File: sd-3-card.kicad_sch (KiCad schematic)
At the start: 20 parts, among them J2 1140084168, Q1 BSS123, Q2 AO3401A, U5 NVT4858HKZ, U6 TPS2116DRLR

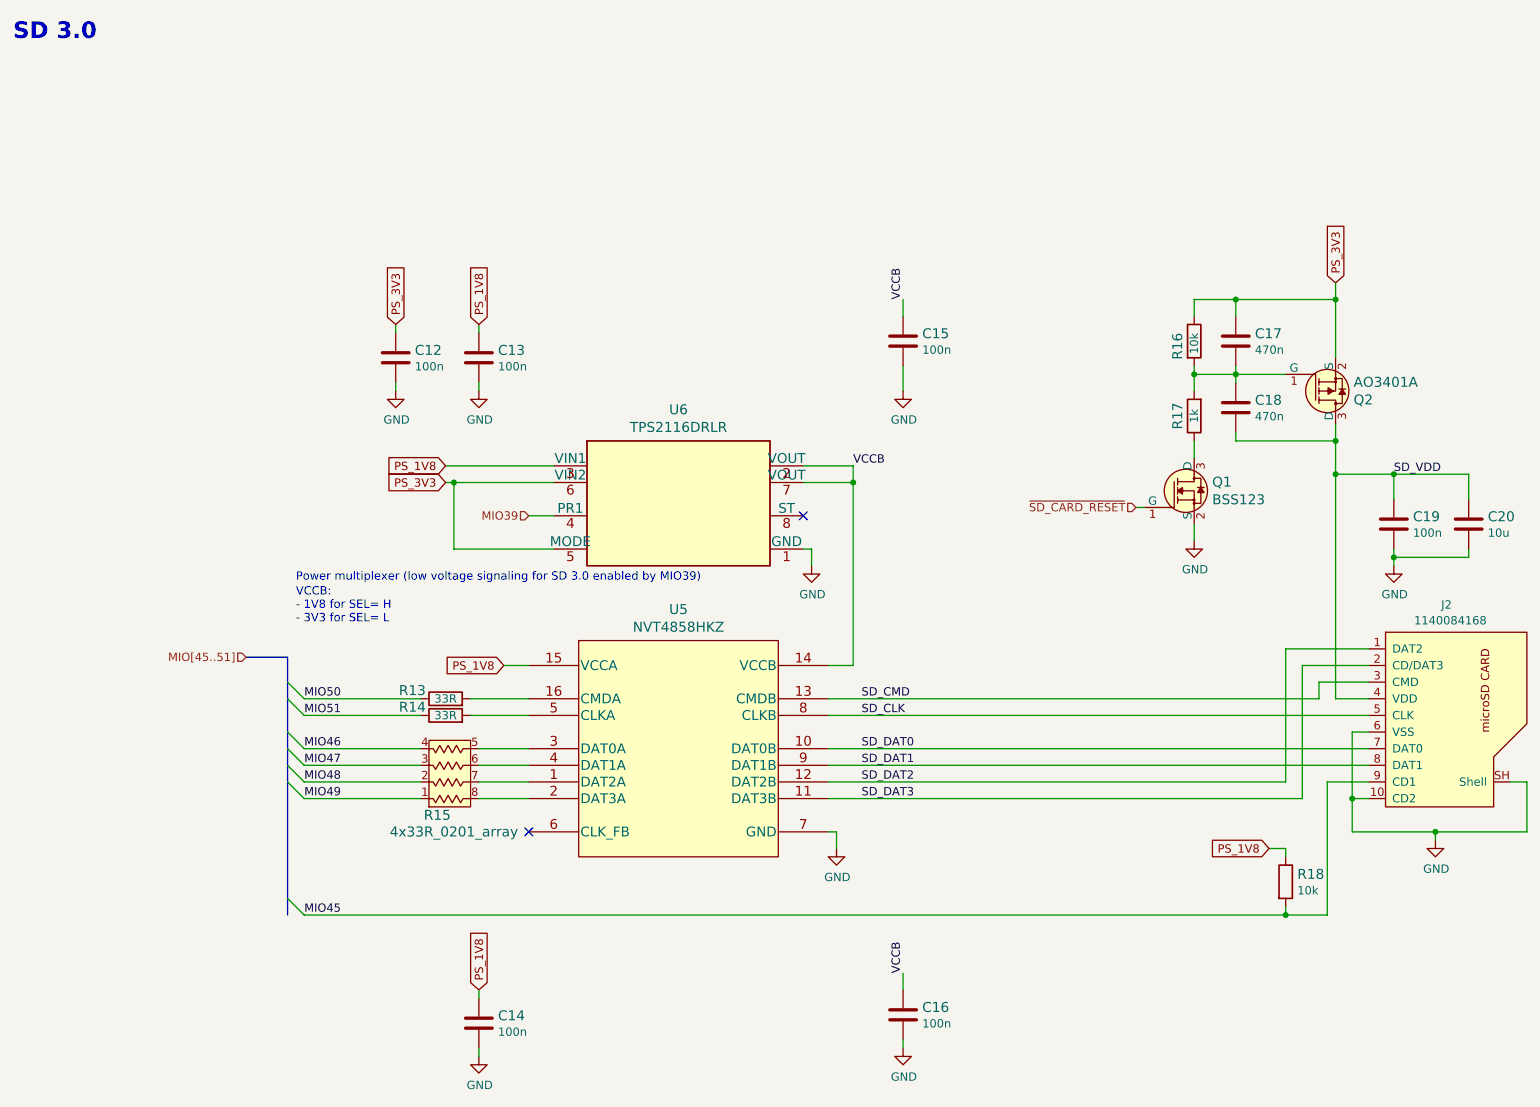
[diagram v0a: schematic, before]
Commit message: Added cosmetic changes to schematics (e.g. position of labels, designators)
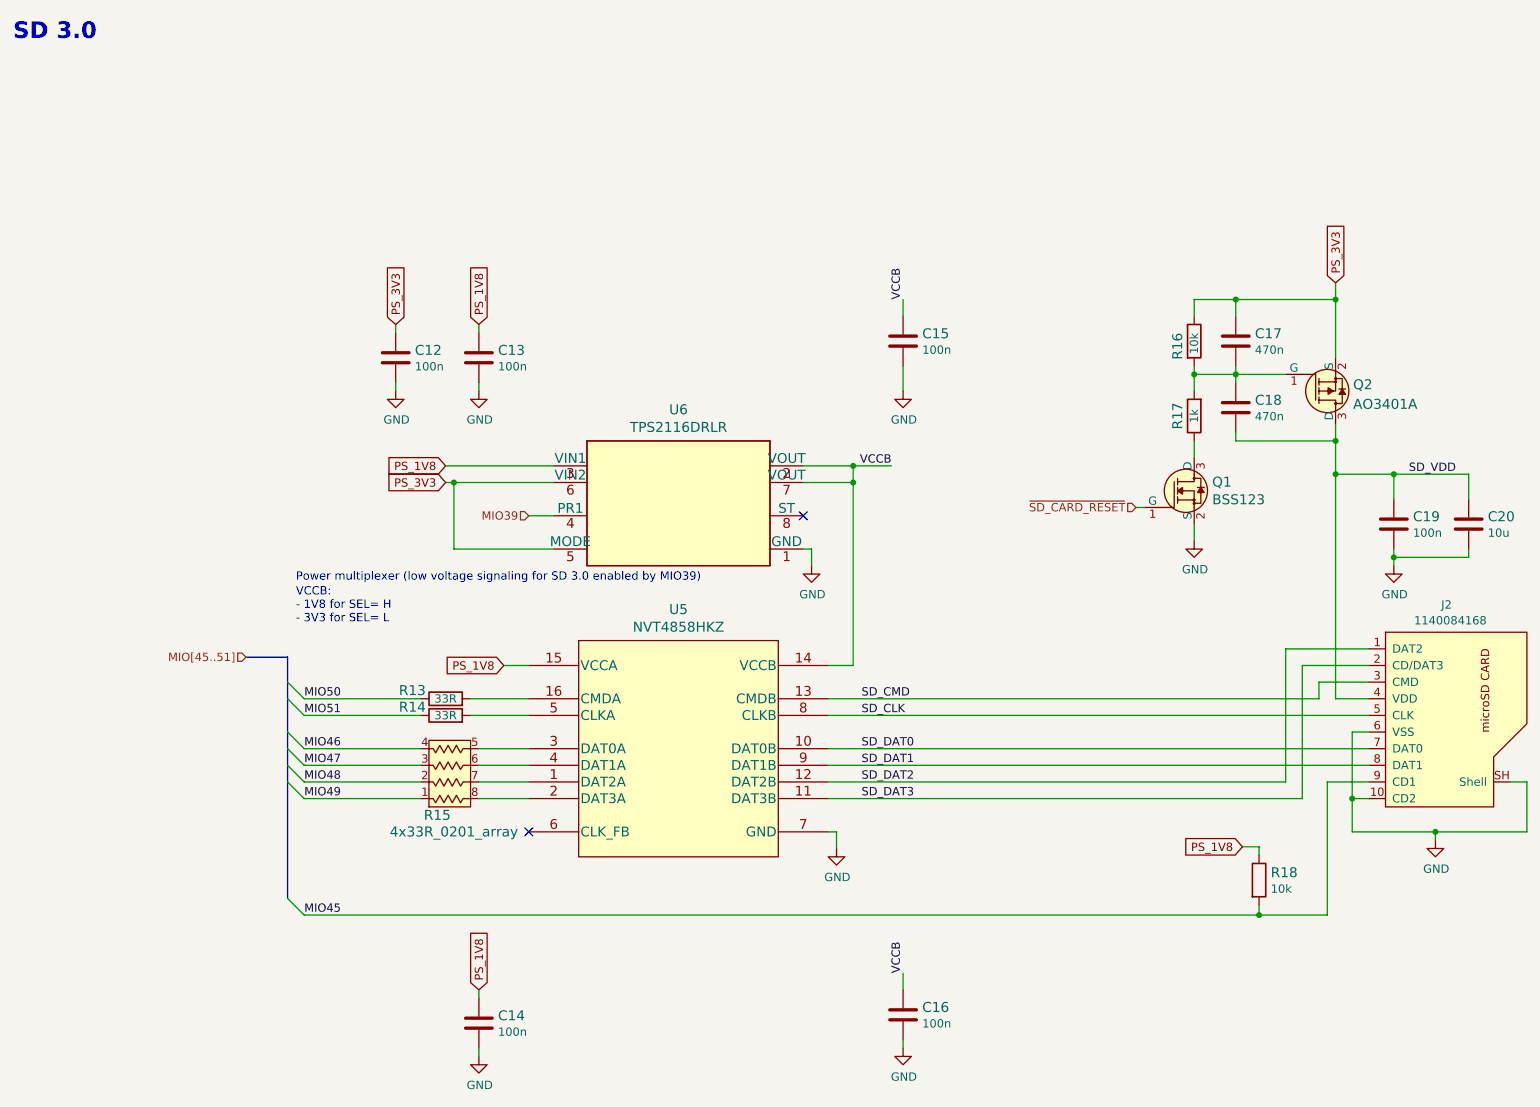
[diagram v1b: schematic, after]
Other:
- moved on the sheet: R18
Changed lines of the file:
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@@
   (junction (at 217.17 58.42) (diameter 0) (color 0 0 0 0)
   )
+  (junction (at 143.51 83.82) (diameter 0) (color 0 0 0 0)
+  )
   (junction (at 226.06 97.79) (diameter 0) (color 0 0 0 0)
   )
-  (junction (at 217.17 85.09) (diameter 0) (color 0 0 0 0)
+  (junction (at 205.486 152.4) (diameter 0) (color 0 0 0 0)
   )
-  (junction (at 209.55 152.4) (diameter 0) (color 0 0 0 0)
+  (junction (at 217.17 85.09) (diameter 0) (color 0 0 0 0)
   )
   (junction (at 226.06 85.09) (diameter 0) (color 0 0 0 0)
@@
     (stroke (width 0) (type default) (color 0 0 0 0))
   )
-  (bus (pts (xy 57.15 149.86) (xy 57.15 152.4))
-    (stroke (width 0) (type default) (color 0 0 0 0))
-  )
-  (wire (pts (xy 209.55 152.4) (xy 209.55 151.13))
+  (wire (pts (xy 205.486 150.876) (xy 205.486 152.4))
     (stroke (width 0) (type default) (color 0 0 0 0))
   )
@@
     (stroke (width 0) (type default) (color 0 0 0 0))
   )
-  (wire (pts (xy 209.55 143.51) (xy 209.55 142.24))
+  (wire (pts (xy 205.486 143.256) (xy 205.486 141.986))
     (stroke (width 0) (type default) (color 0 0 0 0))
   )
@@
     (stroke (width 0) (type default) (color 0 0 0 0))
   )
+  (wire (pts (xy 143.51 83.82) (xy 143.51 86.36))
+    (stroke (width 0) (type default) (color 0 0 0 0))
+  )
   (wire (pts (xy 137.16 99.06) (xy 137.16 96.52))
     (stroke (width 0) (type default) (color 0 0 0 0))
@@
     (stroke (width 0) (type default) (color 0 0 0 0))
   )
-  (wire (pts (xy 209.55 152.4) (xy 215.9 152.4))
+  (wire (pts (xy 59.69 152.4) (xy 205.486 152.4))
     (stroke (width 0) (type default) (color 0 0 0 0))
   )
@@
     (stroke (width 0) (type default) (color 0 0 0 0))
   )
+  (wire (pts (xy 143.51 83.82) (xy 149.352 83.82))
+    (stroke (width 0) (type default) (color 0 0 0 0))
+  )
   (wire (pts (xy 219.71 124.46) (xy 219.71 134.62))
     (stroke (width 0) (type default) (color 0 0 0 0))
@@
     (stroke (width 0) (type default) (color 0 0 0 0))
   )
-  (wire (pts (xy 59.69 152.4) (xy 209.55 152.4))
-    (stroke (width 0) (type default) (color 0 0 0 0))
-  )
   (wire (pts (xy 209.55 111.76) (xy 222.25 111.76))
     (stroke (width 0) (type default) (color 0 0 0 0))
@@
     (stroke (width 0) (type default) (color 0 0 0 0))
   )
-  (wire (pts (xy 207.01 142.24) (xy 209.55 142.24))
+  (wire (pts (xy 202.946 141.986) (xy 205.486 141.986))
     (stroke (width 0) (type default) (color 0 0 0 0))
   )
@@
     (stroke (width 0) (type default) (color 0 0 0 0))
   )
-  (wire (pts (xy 143.51 83.82) (xy 143.51 86.36))
-    (stroke (width 0) (type default) (color 0 0 0 0))
-  )
   (wire (pts (xy 195.58 95.25) (xy 195.58 92.71))
     (stroke (width 0) (type default) (color 0 0 0 0))
@@
     (stroke (width 0) (type default) (color 0 0 0 0))
   )
+  (wire (pts (xy 205.486 152.4) (xy 215.9 152.4))
+    (stroke (width 0) (type default) (color 0 0 0 0))
+  )
   (bus (pts (xy 57.15 132.08) (xy 57.15 149.86))
     (stroke (width 0) (type default) (color 0 0 0 0))
@@
     (effects (font (size 1.27 1.27)) (justify left bottom))
   )
-  (label "SD_VDD" (at 226.06 85.09 0)
+  (label "SD_VDD" (at 228.346 85.09 0)
     (effects (font (size 1.27 1.27)) (justify left bottom))
   )
-  (label "VCCB" (at 143.51 83.82 0)
-    (effects (font (size 1.27 1.27)) (justify left bottom))
+  (label "VCCB" (at 149.352 83.82 180)
+    (effects (font (size 1.27 1.27)) (justify right bottom))
   )
   (label "MIO46" (at 59.69 127 0)
@@
     )
   )
-  (global_label "PS_1V8" (shape input) (at 207.01 142.24 180) (fields_autoplaced)
+  (global_label "PS_1V8" (shape input) (at 202.946 141.986 180) (fields_autoplaced)
     (effects (font (size 1.27 1.27)) (justify right))
-    (property "Intersheet References" "${INTERSHEET_REFS}" (id 0) (at 0 0 0)
+    (property "Intersheet References" "${INTERSHEET_REFS}" (id 0) (at -4.064 -0.254 0)
       (effects (font (size 1.27 1.27)) hide)
     )
@@
     (pin "1")
   )
-  (symbol (lib_id "kria-k26-devboard:R_10k_0402") (at 209.55 147.32 270) (unit 1)
+  (symbol (lib_id "kria-k26-devboard:R_10k_0402") (at 205.486 147.066 270) (unit 1)
     (in_bom yes) (on_board yes)
-    (property "Reference" "R18" (id 0) (at 211.328 146.177 90)
+    (property "Reference" "R18" (id 0) (at 207.264 145.923 90)
       (effects (font (size 1.524 1.524)) (justify left))
     )
-    (property "Value" "R_10k_0402" (id 1) (at 205.74 147.32 0)
+    (property "Value" "R_10k_0402" (id 1) (at 201.676 147.066 0)
       (effects (font (size 1.524 1.524)) hide)
     )
-    (property "Footprint" "kria-k26-devboard-footprints:0402-res" (id 2) (at 214.63 152.4 0)
+    (property "Footprint" "kria-k26-devboard-footprints:0402-res" (id 2) (at 210.566 152.146 0)
       (effects (font (size 1.524 1.524)) (justify left) hide)
     )
-    (property "Datasheet" "" (id 3) (at 209.55 147.32 0)
+    (property "Datasheet" "" (id 3) (at 205.486 147.066 0)
       (effects (font (size 1.27 1.27)) hide)
     )
-    (property "Manufacturer" "VISHAY" (id 4) (at 219.71 152.4 0)
+    (property "Manufacturer" "VISHAY" (id 4) (at 215.646 152.146 0)
       (effects (font (size 1.524 1.524)) (justify left) hide)
     )
-    (property "MPN" "CRCW040210K0FKEDHP" (id 5) (at 217.17 152.4 0)
+    (property "MPN" "CRCW040210K0FKEDHP" (id 5) (at 213.106 152.146 0)
       (effects (font (size 1.524 1.524)) (justify left) hide)
     )
-    (property "Val" "10k" (id 6) (at 211.328 148.6662 90)
+    (property "Val" "10k" (id 6) (at 207.264 148.4122 90)
       (effects (font (size 1.27 1.27)) (justify left))
     )
@@
   )
   (symbol (lib_id "kria-k26-devboard:AO3401A") (at 217.17 72.39 0) (mirror x) (unit 1)
-    (in_bom yes) (on_board yes)
-    (property "Reference" "Q2" (id 0) (at 219.9132 73.7362 0)
+    (in_bom yes) (on_board yes) (fields_autoplaced)
+    (property "Reference" "Q2" (id 0) (at 219.837 71.4138 0)
       (effects (font (size 1.524 1.524)) (justify left))
     )
-    (property "Value" "AO3401A" (id 1) (at 219.9132 71.0438 0)
+    (property "Value" "AO3401A" (id 1) (at 219.837 74.4072 0)
       (effects (font (size 1.524 1.524)) (justify left))
     )

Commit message: Bump date and revision
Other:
- title: SD 3.0 card -> Kria K26 Devboard
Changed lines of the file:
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@@
   (paper "A4")
   (title_block
-    (title "SD 3.0 card")
-    (date "2022-07-25")
-    (rev "1.1.0")
+    (title "Kria K26 Devboard")
+    (date "2023-02-15")
+    (rev "1.1.1")
     (comment 1 "www.antmicro.com")
     (comment 2 "Antmicro Ltd.")

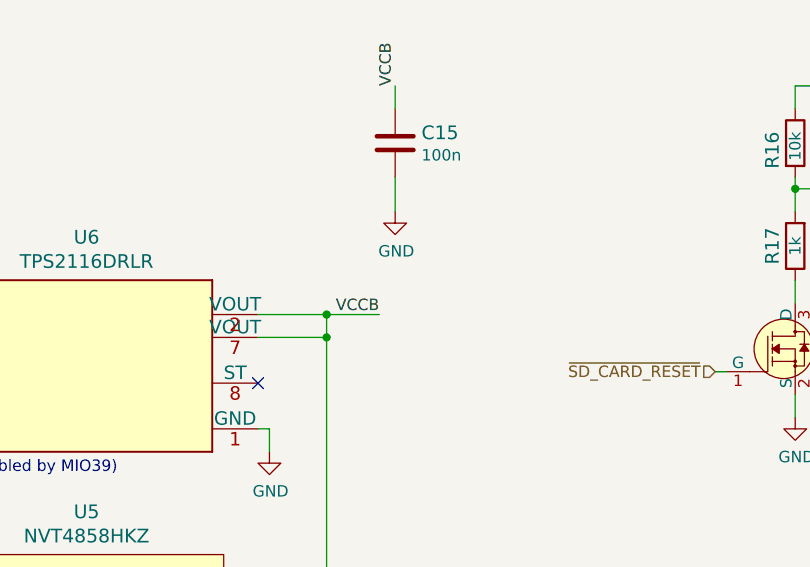
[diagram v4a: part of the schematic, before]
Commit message: Add mandatory pullup to TPS2116 status signal
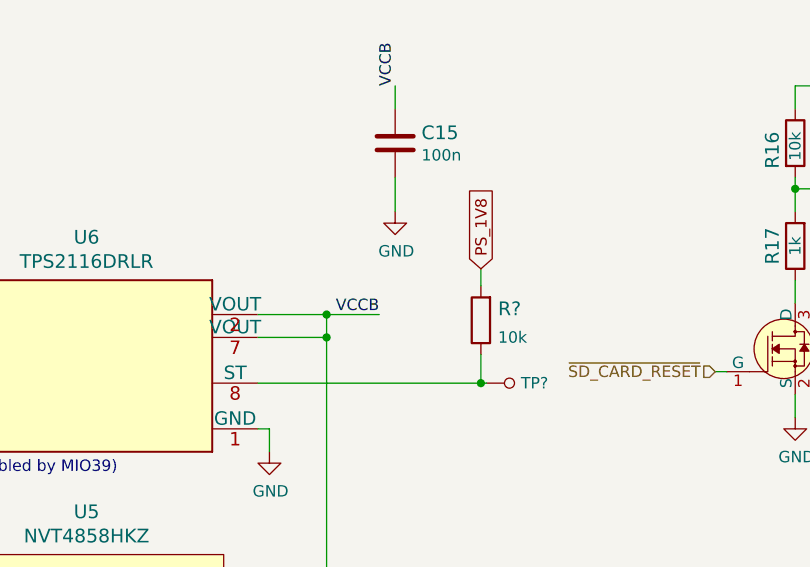
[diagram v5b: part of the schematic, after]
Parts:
- added R?: R_10k_0402, antmicro-footprints:0402-res, symbol antmicroResistors0402:R_10k_0402
- added TP?: TP_SMD_0_75MM, antmicro-footprints:Testpoint_smd_0_75mm, symbol antmicroTestPoints:TP_SMD_0_75MM
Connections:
- net PS_1V8: now also R?.2
- net at U6.8 (ST): now also R?.1, TP?.1
- no-connect marks 2 -> 1
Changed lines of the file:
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@@
   (junction (at 232.41 139.7) (diameter 0) (color 0 0 0 0)
   )
+  (junction (at 160.655 91.44) (diameter 0) (color 0 0 0 0)
+  )
   (junction (at 143.51 86.36) (diameter 0) (color 0 0 0 0)
   )
@@
   )
   (no_connect (at 93.98 139.7))
-  (no_connect (at 135.89 91.44))
   (bus_entry (at 57.15 116.84) (size 2.54 2.54)
     (stroke (width 0) (type default) (color 0 0 0 0))
@@
     (stroke (width 0) (type default) (color 0 0 0 0))
   )
+  (wire (pts (xy 160.655 91.44) (xy 160.655 88.265))
+    (stroke (width 0) (type default) (color 0 0 0 0))
+  )
   (wire (pts (xy 143.51 83.82) (xy 143.51 86.36))
     (stroke (width 0) (type default) (color 0 0 0 0))
@@
     (stroke (width 0) (type default) (color 0 0 0 0))
   )
+  (wire (pts (xy 135.89 91.44) (xy 160.655 91.44))
+    (stroke (width 0) (type default) (color 0 0 0 0))
+  )
   (wire (pts (xy 195.58 69.85) (xy 201.93 69.85))
     (stroke (width 0) (type default) (color 0 0 0 0))
@@
     (stroke (width 0) (type default) (color 0 0 0 0))
   )
+  (wire (pts (xy 160.655 91.44) (xy 161.29 91.44))
+    (stroke (width 0) (type default) (color 0 0 0 0))
+  )
   (bus (pts (xy 57.15 119.38) (xy 57.15 124.46))
     (stroke (width 0) (type default) (color 0 0 0 0))
@@
     (stroke (width 0) (type default) (color 0 0 0 0))
   )
+  (wire (pts (xy 160.655 78.74) (xy 160.655 80.645))
+    (stroke (width 0) (type default) (color 0 0 0 0))
+  )
   (wire (pts (xy 195.58 72.39) (xy 195.58 69.85))
     (stroke (width 0) (type default) (color 0 0 0 0))
@@
     )
   )
+  (global_label "PS_1V8" (shape input) (at 160.655 78.74 90) (fields_autoplaced)
+    (effects (font (size 1.27 1.27)) (justify left))
+    (property "Intersheet References" "${INTERSHEET_REFS}" (id 0) (at 244.475 -2.54 0)
+      (effects (font (size 1.27 1.27)) hide)
+    )
+  )
   (global_label "PS_3V3" (shape input) (at 73.66 62.23 90) (fields_autoplaced)
     (effects (font (size 1.27 1.27)) (justify left))
@@
     )
     (pin "1")
+  )
+  (symbol (lib_id "antmicroResistors0402:R_10k_0402") (at 160.655 84.455 90) (unit 1)
+    (in_bom yes) (on_board yes) (fields_autoplaced)
+    (property "Reference" "R?" (id 0) (at 162.56 83.185 90)
+      (effects (font (size 1.524 1.524)) (justify right))
+    )
+    (property "Value" "R_10k_0402" (id 1) (at 164.465 84.455 0)
+      (effects (font (size 1.524 1.524)) hide)
+    )
+    (property "Footprint" "antmicro-footprints:0402-res" (id 2) (at 155.575 79.375 0)
+      (effects (font (size 1.524 1.524)) (justify left) hide)
+    )
+    (property "Datasheet" "" (id 3) (at 160.655 84.455 0)
+      (effects (font (size 1.27 1.27)) hide)
+    )
+    (property "Manufacturer" "VISHAY" (id 4) (at 150.495 79.375 0)
+      (effects (font (size 1.524 1.524)) (justify left) hide)
+    )
+    (property "MPN" "CRCW040210K0FKEDHP" (id 5) (at 153.035 79.375 0)
+      (effects (font (size 1.524 1.524)) (justify left) hide)
+    )
+    (property "Val" "10k" (id 6) (at 162.56 86.3599 90)
+      (effects (font (size 1.27 1.27)) (justify right))
+    )
+    (pin "1")
+    (pin "2")
+  )
+  (symbol (lib_id "antmicroTestPoints:TP_SMD_0_75MM") (at 163.83 91.44 90) (unit 1)
+    (in_bom yes) (on_board yes) (fields_autoplaced)
+    (property "Reference" "TP?" (id 0) (at 165.1 91.4399 90)
+      (effects (font (size 1.27 1.27)) (justify right))
+    )
+    (property "Value" "TP_SMD_0_75MM" (id 1) (at 166.37 91.44 0)
+      (effects (font (size 1.27 1.27)) hide)
+    )
+    (property "Footprint" "antmicro-footprints:Testpoint_smd_0_75mm" (id 2) (at 158.75 86.36 0)
+      (effects (font (size 1.524 1.524)) (justify left) hide)
+    )
+    (property "Datasheet" "" (id 3) (at 156.21 86.36 0)
+      (effects (font (size 1.524 1.524)) (justify left) hide)
+    )
+    (pin "1")

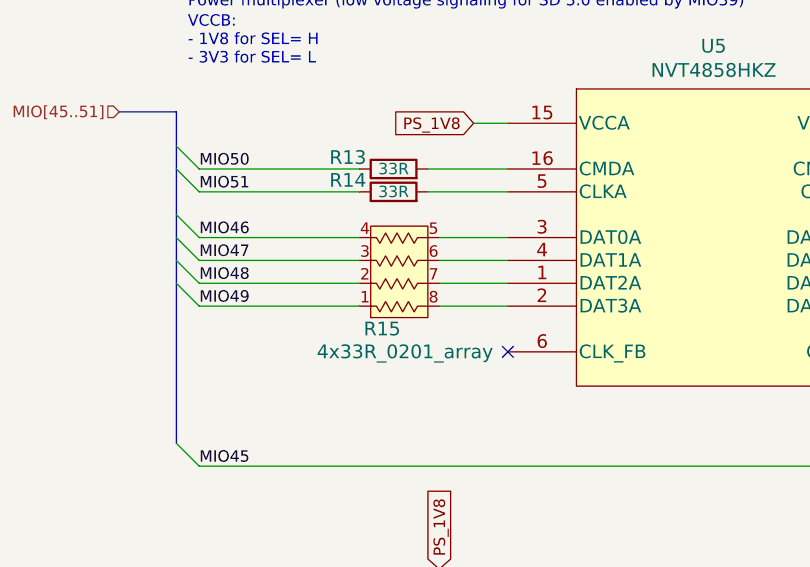
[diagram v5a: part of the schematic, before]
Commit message: Export schematic changes to PCB, fix R15 footprint
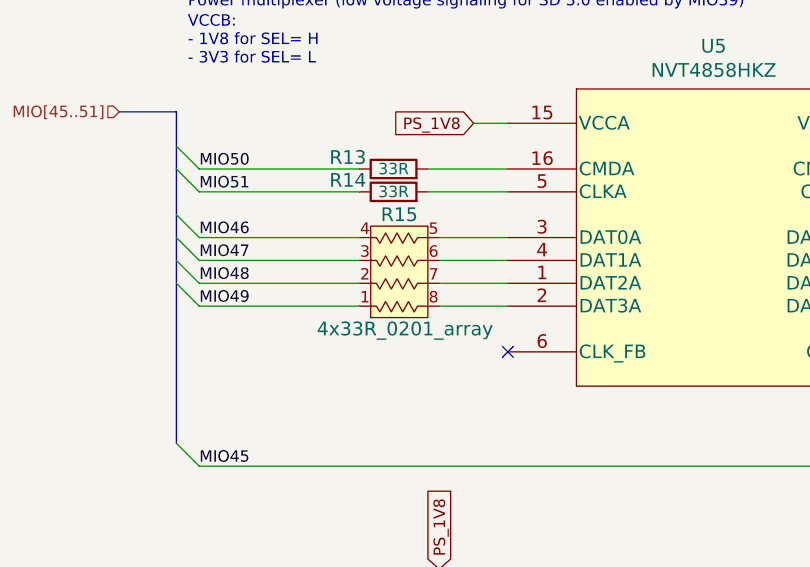
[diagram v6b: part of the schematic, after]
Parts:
- removed R15: 4x33R_0201_array, kria-k26-devboard-footprints:EXB18V, symbol kria-k26-devboard:4x33R_0201_array
- added R15: 4x33R_0201_array, antmicro-footprints:EXB18V, symbol antmicroResistorNetworksArrays:4x33R_0201_array
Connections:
- net MIO46: now also R15.4
- net MIO47: now also R15.3
- net MIO48: now also R15.2
- net MIO49: now also R15.1
- net at U5.1 (DAT2A): now also R15.7
- net at U5.2 (DAT3A): now also R15.8
- net at U5.3 (DAT0A): now also R15.5
- net at U5.4 (DAT1A): now also R15.6
